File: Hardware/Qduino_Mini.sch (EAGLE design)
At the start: 39 parts, among them J1 LiPo, Q1 PFET, U1 ATMEGA32U41:1-LESS_PASTE, U2 MCP73831, U3 MAX17048, U4 AP2112K-3.3TRG-1, U5 MIGHTYQ-L-SILK, Y1 8MHZ

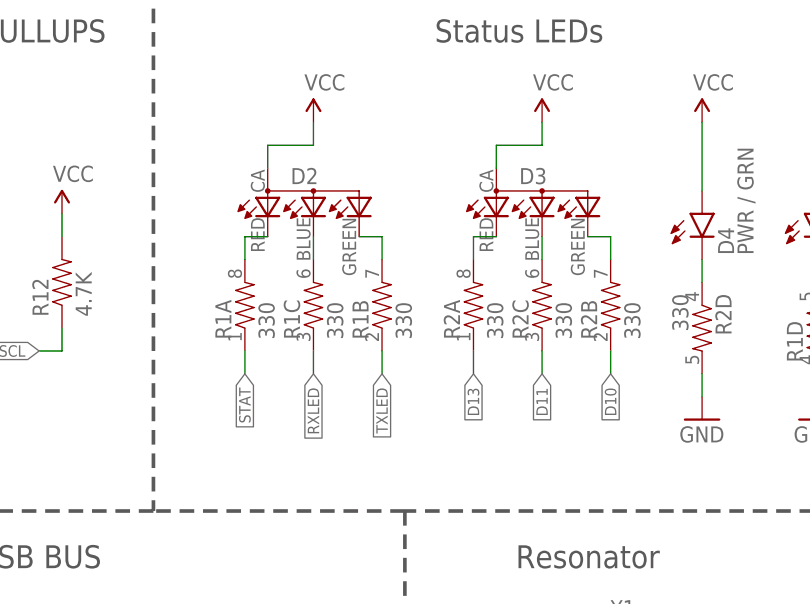
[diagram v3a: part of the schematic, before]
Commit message: Labled LED flags to the colors ther were hooked up to and replaced the RGB LEDs with the footprint for the new part.  STUFF IS BROKEN.
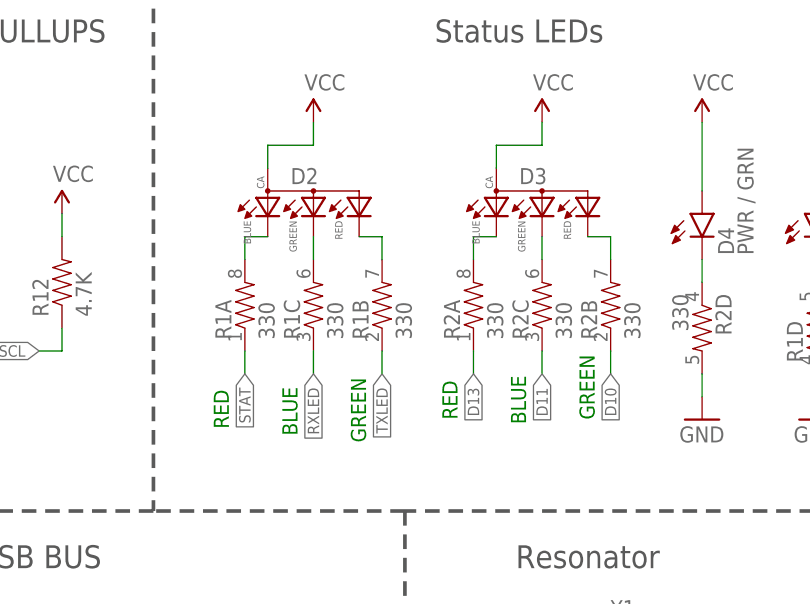
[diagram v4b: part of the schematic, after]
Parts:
- D2, D3: value RGB-LED-CLMVB-FKARGB -> (none); device Spark:RGB-LED-CLMVB-FKARGB -> Testing:0.13_RGB_LEDPLCC
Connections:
- net N$1: now also D2.BLUE; no longer D2.CRED
- net N$2: now also D2.GREEN; no longer D2.CBLUE
- net N$32: now also D3.GREEN; no longer D3.CBLUE
- net N$34: now also D2.RED; no longer D2.CGREEN
- net N$35: now also D3.BLUE; no longer D3.CRED
- net N$37: now also D3.RED; no longer D3.CGREEN
- net VCC: now also D2.ANODE, D3.ANODE; no longer D2.A2, D3.A2
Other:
- note added: "BLUE"
- note added: "GREEN"
- note added: "RED"
- moved on the sheet: D2, D3
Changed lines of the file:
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@@
 <part name="LOGO1" library="SparkFun-Aesthetics" deviceset="OSHW-LOGO" device="S"/>
 <part name="LOGO2" library="SparkFun-Aesthetics" deviceset="SFE_LOGO_FLAME" device=".1_INCH"/>
-<part name="D2" library="Spark" deviceset="RGB-LED-CLMVB-FKA" device="RGB" value=""/>
+<part name="D2" library="Testing" deviceset="0.13_RGB_LED" device="PLCC"/>
 <part name="SUPPLY2" library="SparkFun-Aesthetics" deviceset="VCC" device=""/>
-<part name="D3" library="Spark" deviceset="RGB-LED-CLMVB-FKA" device="RGB" value=""/>
+<part name="D3" library="Testing" deviceset="0.13_RGB_LED" device="PLCC"/>
 <part name="SUPPLY1" library="SparkFun-Aesthetics" deviceset="VCC" device=""/>
 <part name="R1" library="SparkFun-Passives" deviceset="RESISTOR-ARRAY" device="0603-ARV" value="330"/>
@@
 <wire x1="12.7" y1="78.74" x2="12.7" y2="20.32" width="0.4064" layer="97" style="shortdash"/>
 <text x="62.23" y="-43.18" size="2.54" layer="94" ratio="5">Revised by: Brent Wilkins</text>
+<text x="21.082" y="29.464" size="1.6764" layer="91" font="vector" rot="R90">RED</text>
+<text x="46.482" y="30.48" size="1.6764" layer="91" font="vector" rot="R90">RED</text>
+<text x="36.322" y="27.94" size="1.6764" layer="91" font="vector" rot="R90">GREEN</text>
+<text x="61.722" y="30.48" size="1.6764" layer="91" font="vector" rot="R90">GREEN</text>
+<text x="54.102" y="29.972" size="1.6764" layer="91" font="vector" rot="R90">BLUE</text>
+<text x="28.702" y="28.702" size="1.6764" layer="91" font="vector" rot="R90">BLUE</text>
 </plain>
 <instances>
@@
 </segment>
 <segment>
-<pinref part="D2" gate="G$1" pin="A2"/>
+<pinref part="D2" gate="G$1" pin="ANODE"/>
 <wire x1="25.4" y1="58.42" x2="25.4" y2="60.96" width="0.1524" layer="91"/>
 <pinref part="SUPPLY2" gate="G$1" pin="VCC"/>
@@
 </segment>
 <segment>
-<pinref part="D3" gate="G$1" pin="A2"/>
+<pinref part="D3" gate="G$1" pin="ANODE"/>
 <wire x1="50.8" y1="58.42" x2="50.8" y2="60.96" width="0.1524" layer="91"/>
 <pinref part="SUPPLY1" gate="G$1" pin="VCC"/>
@@
 <net name="N$34" class="0">
 <segment>
-<pinref part="D2" gate="G$1" pin="CGREEN"/>
+<pinref part="D2" gate="G$1" pin="RED"/>
 <wire x1="35.56" y1="50.8" x2="38.1" y2="50.8" width="0.1524" layer="91"/>
 <pinref part="R1" gate="B" pin="2"/>
@@
 <net name="N$35" class="0">
 <segment>
-<pinref part="D3" gate="G$1" pin="CRED"/>
+<pinref part="D3" gate="G$1" pin="BLUE"/>
 <wire x1="50.8" y1="50.8" x2="48.26" y2="50.8" width="0.1524" layer="91"/>
 <pinref part="R2" gate="A" pin="2"/>
@@
 <net name="N$37" class="0">
 <segment>
-<pinref part="D3" gate="G$1" pin="CGREEN"/>
+<pinref part="D3" gate="G$1" pin="RED"/>
 <pinref part="R2" gate="B" pin="2"/>
 <wire x1="60.96" y1="50.8" x2="63.5" y2="50.8" width="0.1524" layer="91"/>
@@
 <net name="N$1" class="0">
 <segment>
-<pinref part="D2" gate="G$1" pin="CRED"/>
+<pinref part="D2" gate="G$1" pin="BLUE"/>
 <wire x1="22.86" y1="50.8" x2="25.4" y2="50.8" width="0.1524" layer="91"/>
 <pinref part="R1" gate="A" pin="2"/>
@@
 <net name="N$32" class="0">
 <segment>
-<pinref part="D3" gate="G$1" pin="CBLUE"/>
+<pinref part="D3" gate="G$1" pin="GREEN"/>
 <pinref part="R2" gate="C" pin="2"/>
 <wire x1="55.88" y1="48.26" x2="55.88" y2="50.8" width="0.1524" layer="91"/>
@@
 <segment>
 <pinref part="R1" gate="C" pin="2"/>
-<pinref part="D2" gate="G$1" pin="CBLUE"/>
+<pinref part="D2" gate="G$1" pin="GREEN"/>
 <wire x1="30.48" y1="48.26" x2="30.48" y2="50.8" width="0.1524" layer="91"/>
 </segment>

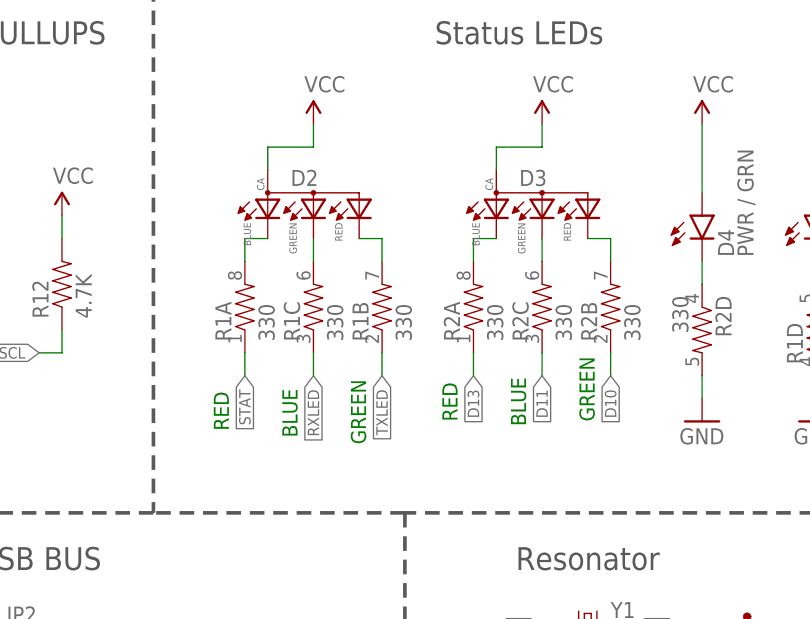
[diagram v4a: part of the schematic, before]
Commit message: Quin reworked the layout to fit the correct footprints for the LEDs he bought
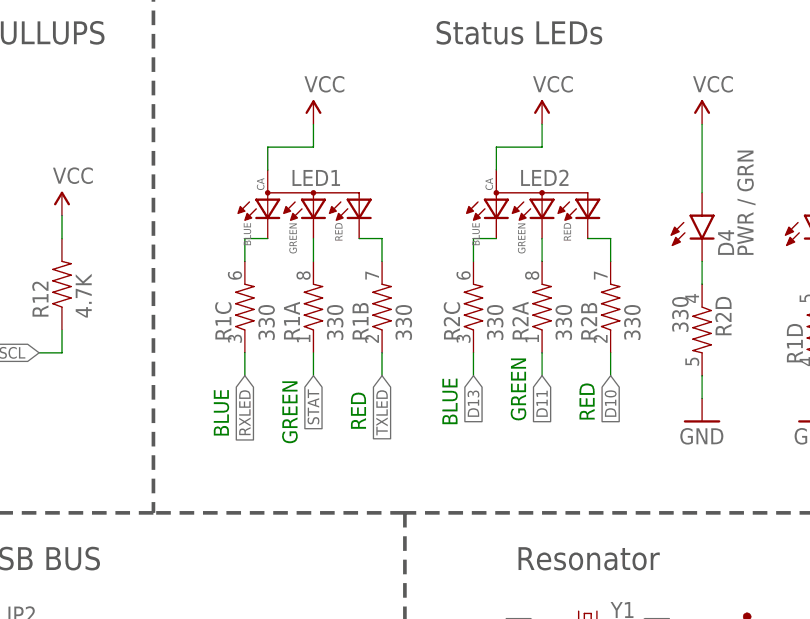
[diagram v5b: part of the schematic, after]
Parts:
- renumbered D2 to LED1, D3 to LED2
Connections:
- removed net N$32: LED2.GREEN, R2C.2
- removed net N$35: LED2.BLUE, R2A.2
- new net N$3: LED2.BLUE, R2C.2
- new net N$8: LED2.GREEN, R2A.2
- net D11: now also R2A.1; no longer R2C.1
- net D13: now also R2C.1; no longer R2A.1
- net N$1: now also R1C.2; no longer R1A.2
- net N$2: now also R1A.2; no longer R1C.2
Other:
- moved on the sheet: R1A, R1C, R2A, R2C
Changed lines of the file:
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@@
 <?xml version="1.0" encoding="utf-8"?>
 <!DOCTYPE eagle SYSTEM "eagle.dtd">
-<eagle version="7.2.0">
+<eagle version="7.1.0">
 <drawing>
 <settings>
@@
 <part name="LOGO1" library="SparkFun-Aesthetics" deviceset="OSHW-LOGO" device="S"/>
 <part name="LOGO2" library="SparkFun-Aesthetics" deviceset="SFE_LOGO_FLAME" device=".1_INCH"/>
-<part name="D2" library="Testing" deviceset="0.13_RGB_LED" device="PLCC"/>
+<part name="LED1" library="Testing" deviceset="0.13_RGB_LED" device="PLCC"/>
 <part name="SUPPLY2" library="SparkFun-Aesthetics" deviceset="VCC" device=""/>
-<part name="D3" library="Testing" deviceset="0.13_RGB_LED" device="PLCC"/>
+<part name="LED2" library="Testing" deviceset="0.13_RGB_LED" device="PLCC"/>
 <part name="SUPPLY1" library="SparkFun-Aesthetics" deviceset="VCC" device=""/>
 <part name="R1" library="SparkFun-Passives" deviceset="RESISTOR-ARRAY" device="0603-ARV" value="330"/>
@@
 <wire x1="12.7" y1="78.74" x2="12.7" y2="20.32" width="0.4064" layer="97" style="shortdash"/>
 <text x="62.23" y="-43.18" size="2.54" layer="94" ratio="5">Revised by: Brent Wilkins</text>
-<text x="21.082" y="29.464" size="1.6764" layer="91" font="vector" rot="R90">RED</text>
-<text x="46.482" y="30.48" size="1.6764" layer="91" font="vector" rot="R90">RED</text>
-<text x="36.322" y="27.94" size="1.6764" layer="91" font="vector" rot="R90">GREEN</text>
-<text x="61.722" y="30.48" size="1.6764" layer="91" font="vector" rot="R90">GREEN</text>
-<text x="54.102" y="29.972" size="1.6764" layer="91" font="vector" rot="R90">BLUE</text>
-<text x="28.702" y="28.702" size="1.6764" layer="91" font="vector" rot="R90">BLUE</text>
+<text x="36.322" y="29.464" size="1.6764" layer="91" font="vector" rot="R90">RED</text>
+<text x="61.722" y="30.48" size="1.6764" layer="91" font="vector" rot="R90">RED</text>
+<text x="28.702" y="27.94" size="1.6764" layer="91" font="vector" rot="R90">GREEN</text>
+<text x="54.102" y="30.48" size="1.6764" layer="91" font="vector" rot="R90">GREEN</text>
+<text x="46.482" y="29.972" size="1.6764" layer="91" font="vector" rot="R90">BLUE</text>
+<text x="21.082" y="28.702" size="1.6764" layer="91" font="vector" rot="R90">BLUE</text>
 </plain>
 <instances>
@@
 <instance part="LOGO1" gate="G$1" x="-35.56" y="-38.1"/>
 <instance part="LOGO2" gate="G$1" x="-17.78" y="-30.48"/>
-<instance part="D2" gate="G$1" x="30.48" y="53.34"/>
+<instance part="LED1" gate="G$1" x="30.48" y="53.34"/>
 <instance part="SUPPLY2" gate="G$1" x="30.48" y="63.5"/>
-<instance part="D3" gate="G$1" x="55.88" y="53.34"/>
+<instance part="LED2" gate="G$1" x="55.88" y="53.34"/>
 <instance part="SUPPLY1" gate="G$1" x="55.88" y="63.5"/>
-<instance part="R1" gate="A" x="22.86" y="43.18" rot="R90"/>
+<instance part="R1" gate="A" x="30.48" y="43.18" rot="R90"/>
 <instance part="R1" gate="B" x="38.1" y="43.18" rot="R90"/>
-<instance part="R1" gate="C" x="30.48" y="43.18" rot="R90"/>
+<instance part="R1" gate="C" x="22.86" y="43.18" rot="R90"/>
 <instance part="R1" gate="D" x="86.36" y="40.64" rot="R90"/>
-<instance part="R2" gate="A" x="48.26" y="43.18" rot="R90"/>
+<instance part="R2" gate="A" x="55.88" y="43.18" rot="R90"/>
 <instance part="R2" gate="B" x="63.5" y="43.18" rot="R90"/>
-<instance part="R2" gate="C" x="55.88" y="43.18" rot="R90"/>
+<instance part="R2" gate="C" x="48.26" y="43.18" rot="R90"/>
 <instance part="R2" gate="D" x="73.66" y="40.64" rot="R270"/>
 <instance part="JP3" gate="G$1" x="-50.8" y="-7.62"/>
@@
 <segment>
 <pinref part="R1" gate="C" pin="1"/>
-<wire x1="30.48" y1="38.1" x2="30.48" y2="35.56" width="0.1524" layer="91"/>
-<label x="30.48" y="35.56" size="1.27" layer="95" rot="R270" xref="yes"/>
+<wire x1="22.86" y1="38.1" x2="22.86" y2="35.56" width="0.1524" layer="91"/>
+<label x="22.86" y="35.56" size="1.27" layer="95" rot="R270" xref="yes"/>
 </segment>
 </net>
@@
 <segment>
 <pinref part="R1" gate="A" pin="1"/>
-<wire x1="22.86" y1="38.1" x2="22.86" y2="35.56" width="0.1524" layer="91"/>
-<label x="22.86" y="35.56" size="1.27" layer="95" rot="R270" xref="yes"/>
+<wire x1="30.48" y1="38.1" x2="30.48" y2="35.56" width="0.1524" layer="91"/>
+<label x="30.48" y="35.56" size="1.27" layer="95" rot="R270" xref="yes"/>
 </segment>
 </net>
@@
 </segment>
 <segment>
-<pinref part="D2" gate="G$1" pin="ANODE"/>
+<pinref part="LED1" gate="G$1" pin="ANODE"/>
 <wire x1="25.4" y1="58.42" x2="25.4" y2="60.96" width="0.1524" layer="91"/>
 <pinref part="SUPPLY2" gate="G$1" pin="VCC"/>
@@
 </segment>
 <segment>
-<pinref part="D3" gate="G$1" pin="ANODE"/>
+<pinref part="LED2" gate="G$1" pin="ANODE"/>
 <wire x1="50.8" y1="58.42" x2="50.8" y2="60.96" width="0.1524" layer="91"/>
 <pinref part="SUPPLY1" gate="G$1" pin="VCC"/>
@@
 </segment>
 <segment>
-<pinref part="R2" gate="C" pin="1"/>
+<pinref part="R2" gate="A" pin="1"/>
 <wire x1="55.88" y1="38.1" x2="55.88" y2="35.56" width="0.1524" layer="91"/>
 <label x="55.88" y="35.56" size="1.27" layer="95" rot="R270" xref="yes"/>
@@
 </segment>
 <segment>
-<pinref part="R2" gate="A" pin="1"/>
+<pinref part="R2" gate="C" pin="1"/>
 <wire x1="48.26" y1="38.1" x2="48.26" y2="35.56" width="0.1524" layer="91"/>
 <label x="48.26" y="35.56" size="1.27" layer="95" rot="R270" xref="yes"/>
@@
 <net name="N$34" class="0">
 <segment>
-<pinref part="D2" gate="G$1" pin="RED"/>
+<pinref part="LED1" gate="G$1" pin="RED"/>
 <wire x1="35.56" y1="50.8" x2="38.1" y2="50.8" width="0.1524" layer="91"/>
 <pinref part="R1" gate="B" pin="2"/>
@@
 </segment>
 </net>
-<net name="N$35" class="0">
-<segment>
-<pinref part="D3" gate="G$1" pin="BLUE"/>
-<wire x1="50.8" y1="50.8" x2="48.26" y2="50.8" width="0.1524" layer="91"/>
-<pinref part="R2" gate="A" pin="2"/>
-<wire x1="48.26" y1="50.8" x2="48.26" y2="48.26" width="0.1524" layer="91"/>
-</segment>
-</net>
 <net name="N$37" class="0">
 <segment>
-<pinref part="D3" gate="G$1" pin="RED"/>
+<pinref part="LED2" gate="G$1" pin="RED"/>
 <pinref part="R2" gate="B" pin="2"/>
 <wire x1="60.96" y1="50.8" x2="63.5" y2="50.8" width="0.1524" layer="91"/>
@@
 </segment>
 </net>
-<net name="N$1" class="0">
-<segment>
-<pinref part="D2" gate="G$1" pin="BLUE"/>
-<wire x1="22.86" y1="50.8" x2="25.4" y2="50.8" width="0.1524" layer="91"/>
-<pinref part="R1" gate="A" pin="2"/>
-<wire x1="22.86" y1="48.26" x2="22.86" y2="50.8" width="0.1524" layer="91"/>
-</segment>
-</net>
-<net name="N$32" class="0">
-<segment>
-<pinref part="D3" gate="G$1" pin="GREEN"/>
-<pinref part="R2" gate="C" pin="2"/>
-<wire x1="55.88" y1="48.26" x2="55.88" y2="50.8" width="0.1524" layer="91"/>
-</segment>
-</net>
 <net name="N$5" class="0">
 <segment>
@@
 </segment>
 </net>
-<net name="N$2" class="0">
-<segment>
-<pinref part="R1" gate="C" pin="2"/>
-<pinref part="D2" gate="G$1" pin="GREEN"/>
-<wire x1="30.48" y1="48.26" x2="30.48" y2="50.8" width="0.1524" layer="91"/>
-</segment>
-</net>
 <net name="N$4" class="0">
 <segment>
@@
 </segment>
 </net>
+<net name="N$3" class="0">
+<segment>
+<pinref part="LED2" gate="G$1" pin="BLUE"/>
+<pinref part="R2" gate="C" pin="2"/>
+<wire x1="50.8" y1="50.8" x2="48.26" y2="50.8" width="0.1524" layer="91"/>
+<wire x1="48.26" y1="50.8" x2="48.26" y2="48.26" width="0.1524" layer="91"/>
+</segment>
+</net>
+<net name="N$8" class="0">
+<segment>
+<pinref part="LED2" gate="G$1" pin="GREEN"/>
+<pinref part="R2" gate="A" pin="2"/>
+<wire x1="55.88" y1="50.8" x2="55.88" y2="48.26" width="0.1524" layer="91"/>
+</segment>
+</net>
+<net name="N$1" class="0">
+<segment>
+<pinref part="LED1" gate="G$1" pin="BLUE"/>
+<pinref part="R1" gate="C" pin="2"/>
+<wire x1="25.4" y1="50.8" x2="22.86" y2="50.8" width="0.1524" layer="91"/>
+<wire x1="22.86" y1="50.8" x2="22.86" y2="48.26" width="0.1524" layer="91"/>
+</segment>
+</net>
+<net name="N$2" class="0">
+<segment>
+<pinref part="LED1" gate="G$1" pin="GREEN"/>
+<pinref part="R1" gate="A" pin="2"/>
+<wire x1="30.48" y1="50.8" x2="30.48" y2="48.26" width="0.1524" layer="91"/>
+</segment>
+</net>
